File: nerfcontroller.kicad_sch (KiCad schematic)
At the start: 39 parts, among them J1 Conn_01x02_Pin, J10 Conn_01x03_Pin, J11 Conn_01x03_Pin, J12 Conn_01x03_Pin, J13 Conn_01x03_Pin, J14 Conn_01x03_Pin, J15 Conn_01x02_Pin, J16 Conn_01x02_Pin, J2 Conn_01x02_Pin, J3 Conn_01x02_Pin, J4 Conn_01x02_Pin, J5 Conn_01x03_Pin, J6 Conn_01x03_Pin, J7 Conn_01x03_Pin, J8 Conn_01x03_Pin, J9 Conn_01x03_Pin, Q1 IRL530, Q2 IRL530, Q3 IRL530, Q4 IRL530, U1 LM7805_TO220

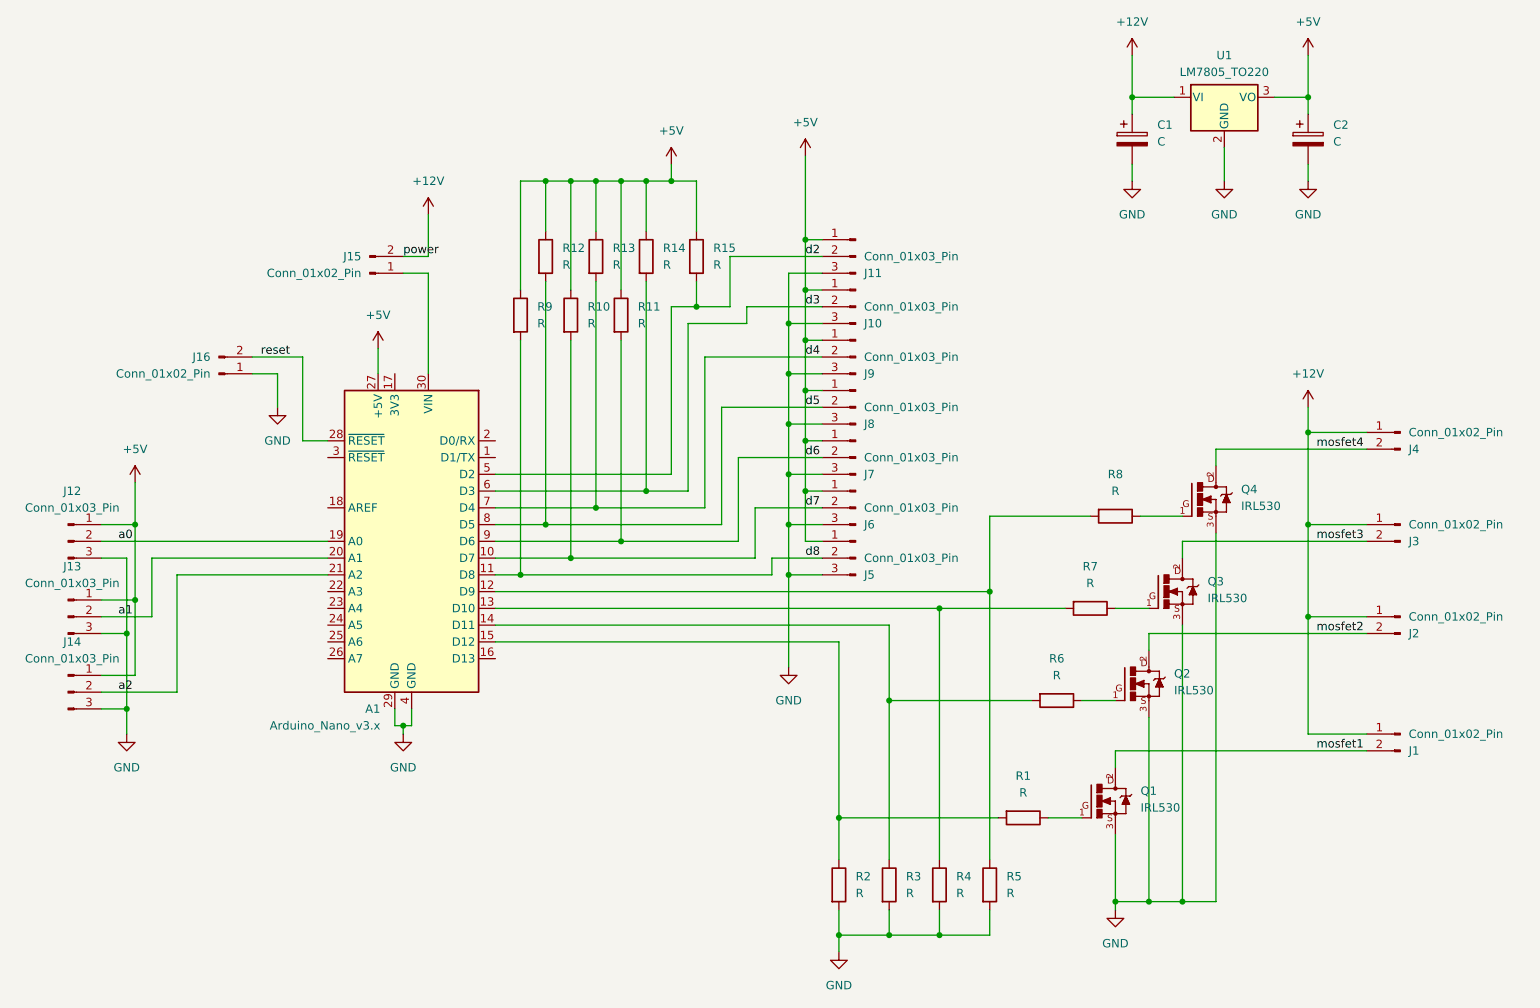
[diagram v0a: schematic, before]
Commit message: added resistor values for mosfets
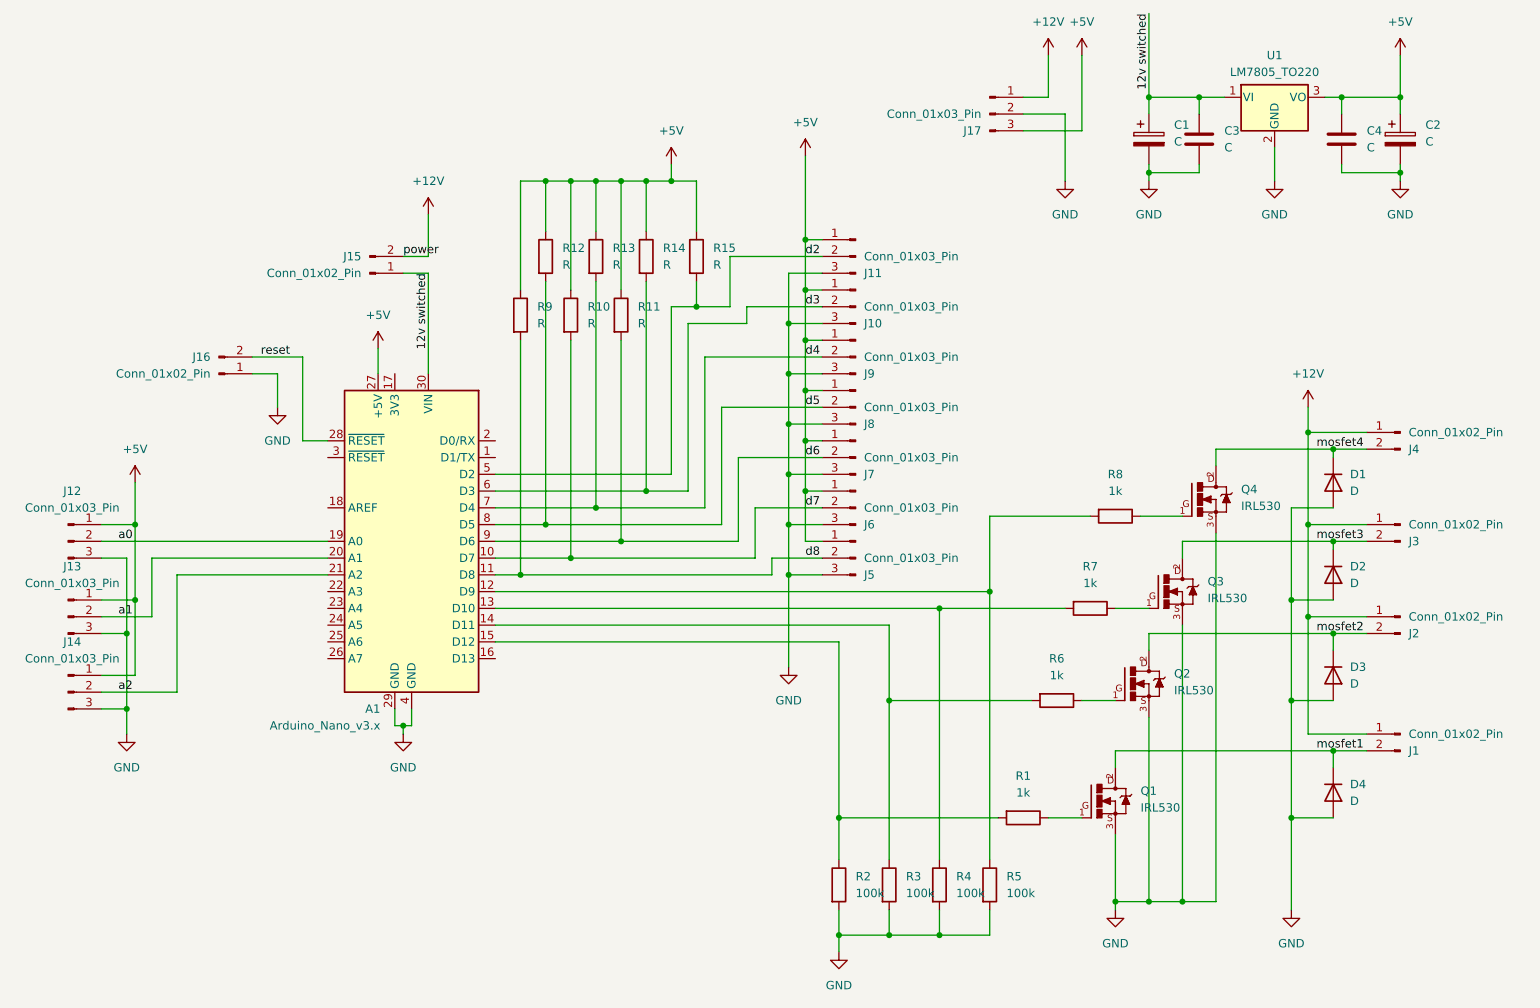
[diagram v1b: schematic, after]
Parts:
- added C3, C4: C, Capacitor_SMD:C_0805_2012Metric_Pad1.18x1.45mm_HandSolder, symbol Device:C
- added D1, D2, D3, D4: D, Diode_SMD:D_0805_2012Metric_Pad1.15x1.40mm_HandSolder, symbol Device:D
- added J17: Conn_01x03_Pin, Connector_PinHeader_2.54mm:PinHeader_1x03_P2.54mm_Vertical, symbol Connector:Conn_01x03_Pin
- R1, R6, R7, R8: value R -> 1k
- R2, R3, R4, R5: value R -> 100k
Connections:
- net +12V: now also J17.1 (Pin_1); no longer C1.1, U1.1 (VI)
- net +5V: now also C4.1, J17.3 (Pin_3)
- net GND: now also C3.2, C4.2, D1.2 (A), D2.2 (A), D3.2 (A), D4.2 (A), J17.2 (Pin_2)
- net mosfet1: now also D4.1 (K)
- net mosfet2: now also D3.1 (K)
- net mosfet3: now also D2.1 (K)
- net mosfet4: now also D1.1 (K)
- net 12v switched: now reaches A1.30 (VIN), J15.1 (Pin_1)
- net 12v switched: now also C1.1, U1.1 (VI), C3.1
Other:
- moved on the sheet: C1, C2, U1

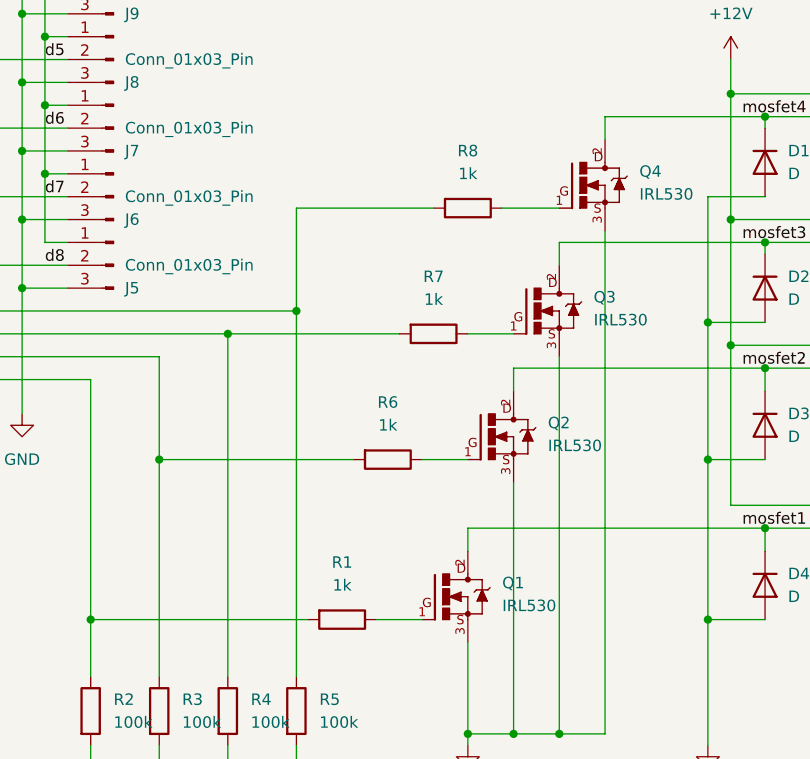
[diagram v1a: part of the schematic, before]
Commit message: corrected resistor values + silkscreen goofs
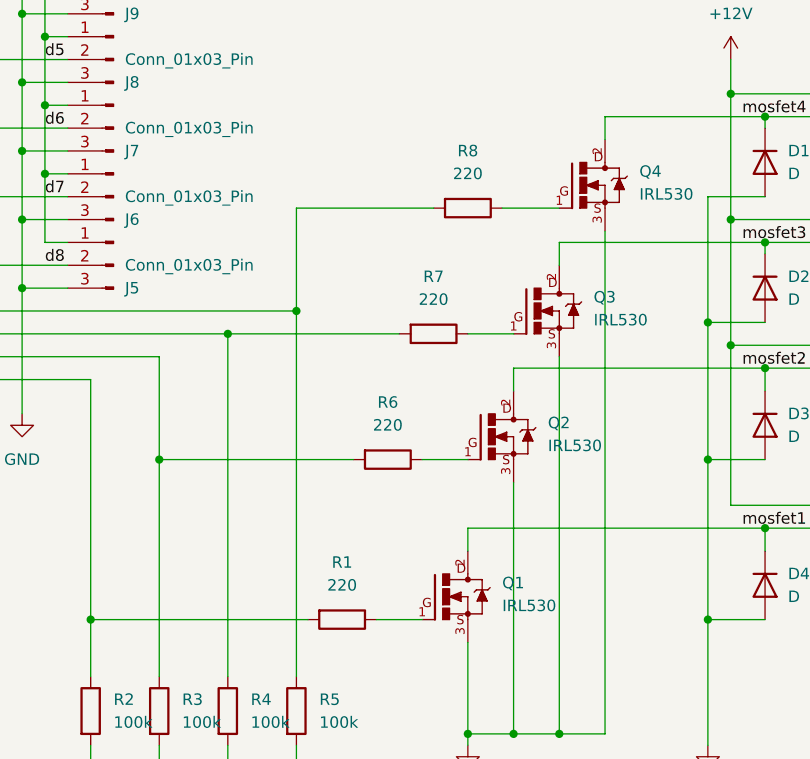
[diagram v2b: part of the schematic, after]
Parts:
- R1, R6, R7, R8: value 1k -> 220
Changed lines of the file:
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@@
       (effects (font (size 1.27 1.27)))
     )
-    (property "Value" "1k" (at 212.09 102.87 90)
+    (property "Value" "220" (at 212.09 102.87 90)
       (effects (font (size 1.27 1.27)))
     )
@@
       (effects (font (size 1.27 1.27)))
     )
-    (property "Value" "1k" (at 215.9 88.9 90)
+    (property "Value" "220" (at 215.9 88.9 90)
       (effects (font (size 1.27 1.27)))
     )
@@
       (effects (font (size 1.27 1.27)))
     )
-    (property "Value" "1k" (at 201.93 134.62 90)
+    (property "Value" "220" (at 201.93 134.62 90)
       (effects (font (size 1.27 1.27)))
     )
@@
       (effects (font (size 1.27 1.27)))
     )
-    (property "Value" "1k" (at 207.01 116.84 90)
-      (effects (font (size 1.27 1.27)))
-    )
+    (property "Value" "220" (at 207.01 116.84 90)
+      (effects (font (size 1.27 1.27)))
+    )

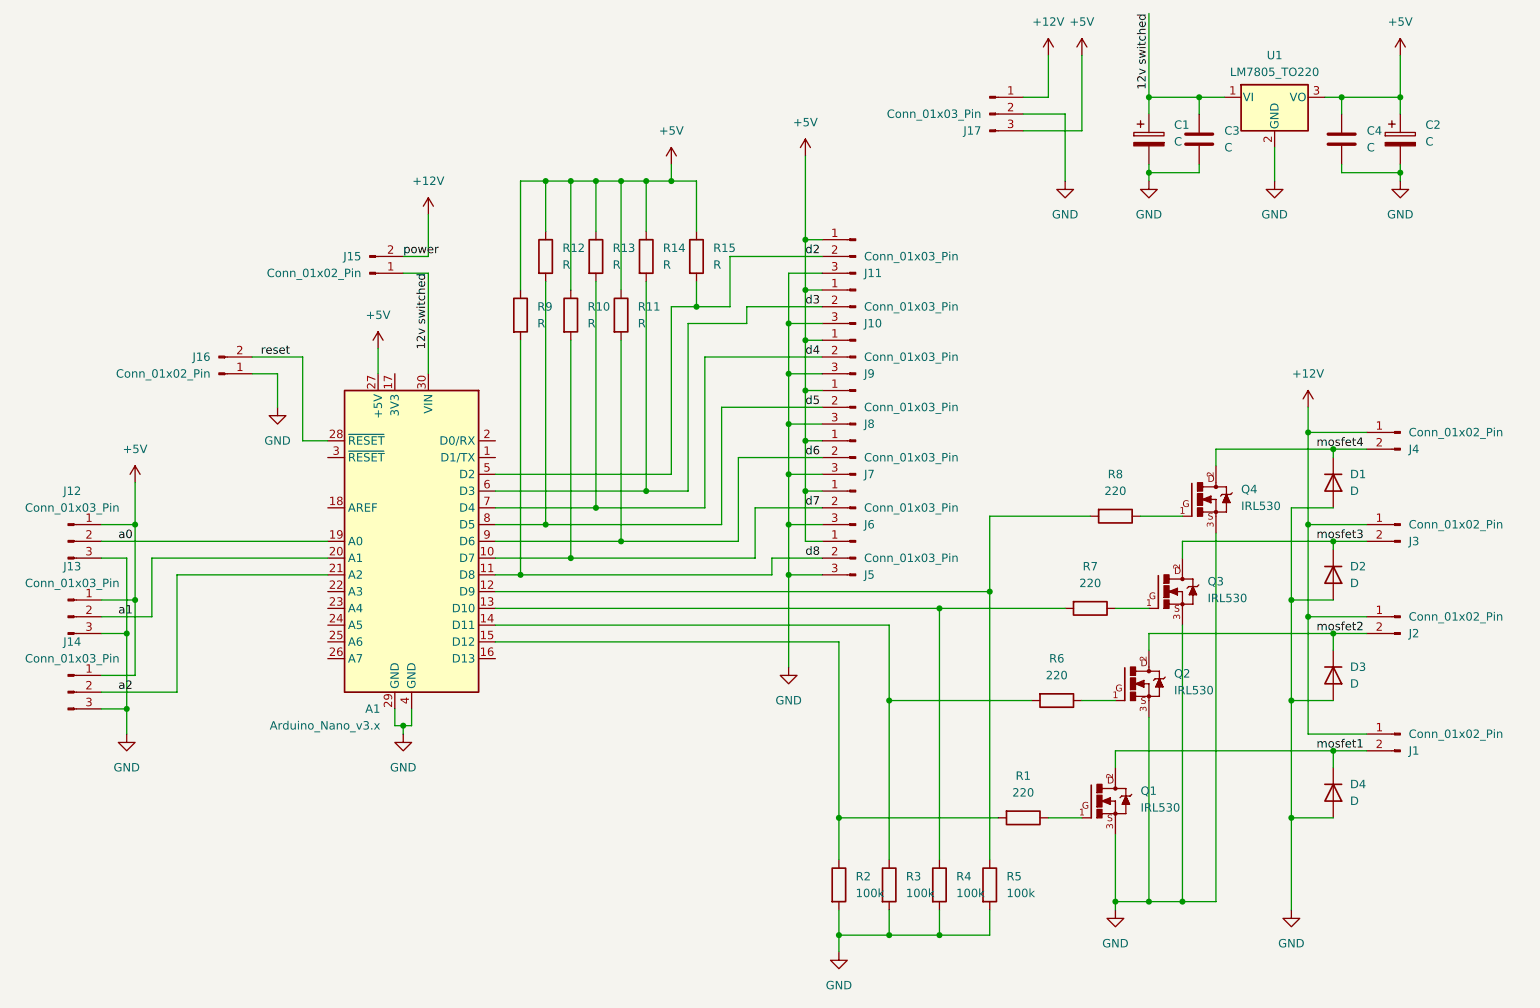
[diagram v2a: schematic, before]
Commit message: added mosfet drivers and sot23 diodes
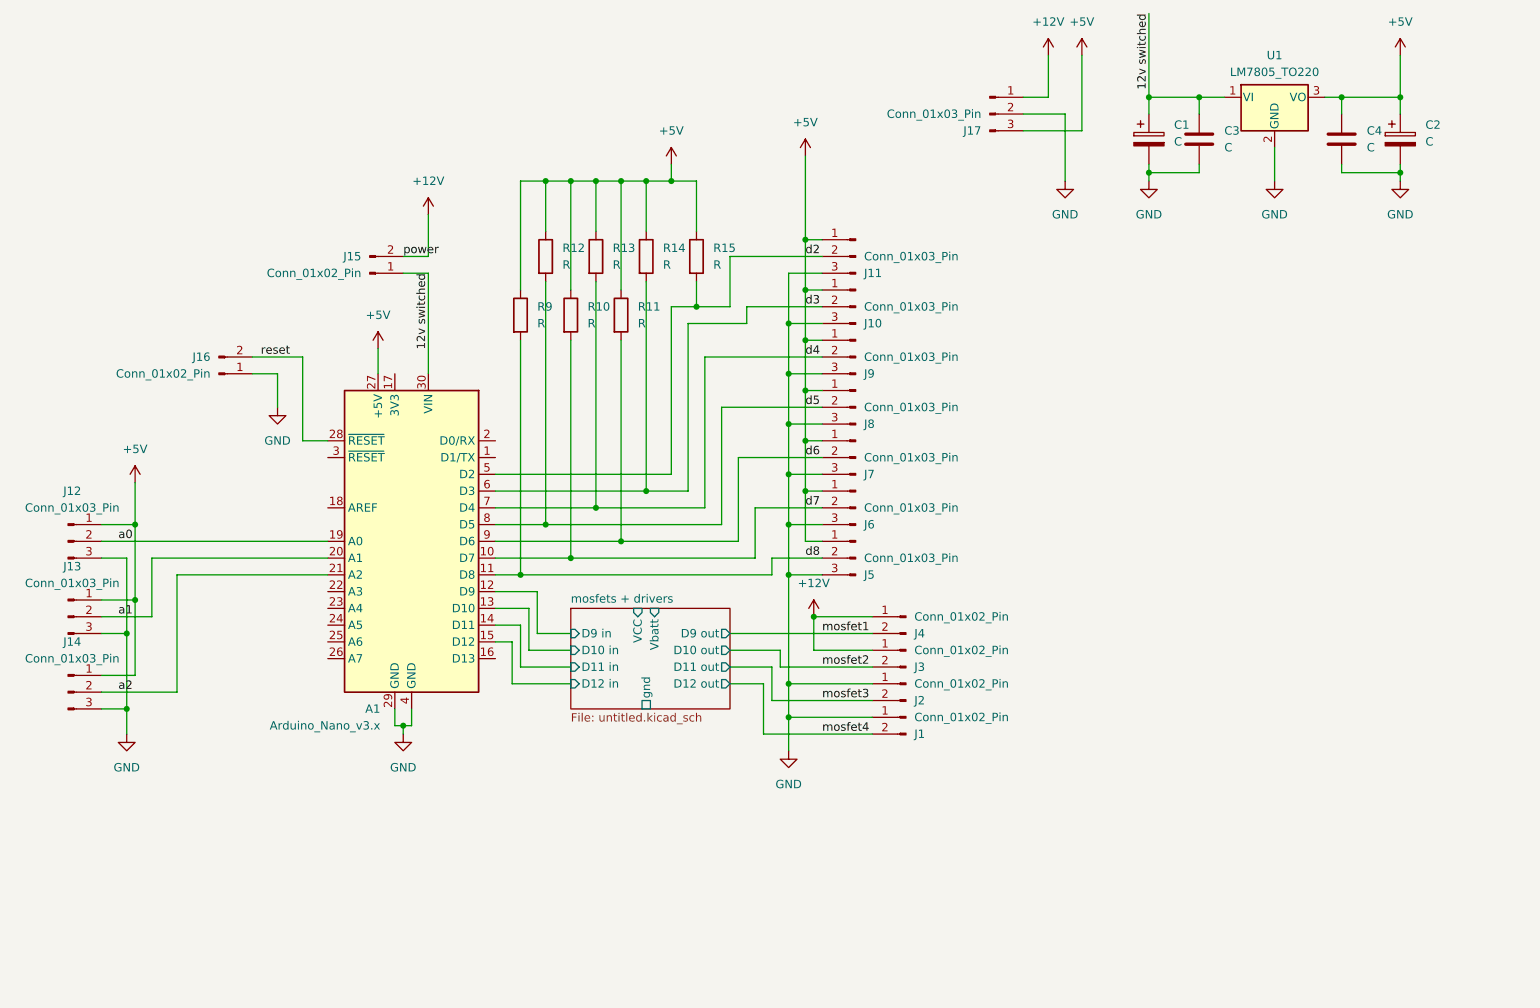
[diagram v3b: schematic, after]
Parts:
- removed D1, D2, D3, D4: D, Diode_SMD:D_0805_2012Metric_Pad1.15x1.40mm_HandSolder, symbol Device:D
- removed Q1, Q2, Q3, Q4: IRL530, Package_TO_SOT_THT:TO-220-3_Vertical, symbol IRL530:IRL530
- removed R1, R6, R7, R8: 220, Resistor_SMD:R_0805_2012Metric, symbol Device:R
- removed R2, R3, R4, R5: 100k, Resistor_SMD:R_0805_2012Metric, symbol Device:R
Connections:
- net +12V: no longer J1.1 (Pin_1), J2.1 (Pin_1)
- net GND: now also J1.1 (Pin_1), J2.1 (Pin_1)
- net mosfet1: now also J4.2 (Pin_2); no longer J1.2 (Pin_2)
- net mosfet2: now also J3.2 (Pin_2); no longer J2.2 (Pin_2)
- net mosfet3: now also J2.2 (Pin_2); no longer J3.2 (Pin_2)
- net mosfet4: now also J1.2 (Pin_2); no longer J4.2 (Pin_2)
- net mosfets + drivers/D11 in: now reaches A1.14 (D11)
- net mosfets + drivers/D10 in: now reaches A1.13 (D10)
- net mosfets + drivers/D9 in: now reaches A1.12 (D9)
- net mosfets + drivers/D12 in: now reaches A1.15 (D12)
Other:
- added sheet mosfets + drivers (untitled.kicad_sch)
